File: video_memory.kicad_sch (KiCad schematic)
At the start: 23 parts

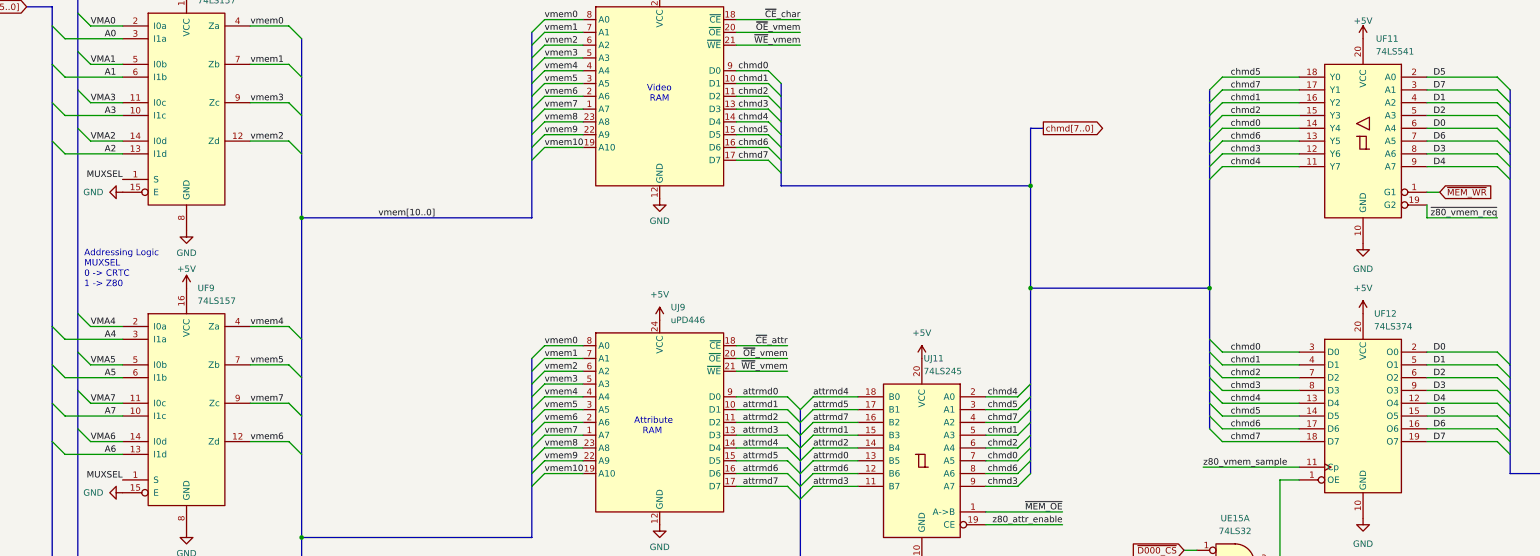
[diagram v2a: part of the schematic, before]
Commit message: pcb: finished IC routing
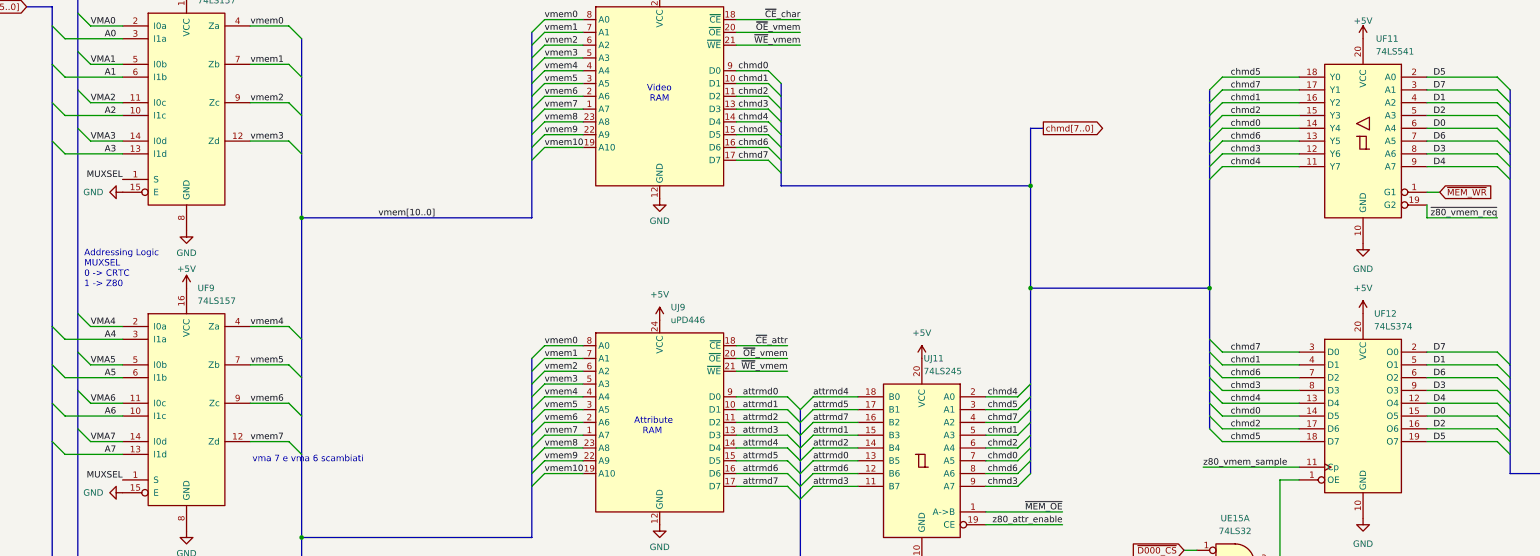
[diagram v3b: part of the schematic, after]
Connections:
- net A2: now also UF8.10 (I1c); no longer UF8.13 (I1d)
- net A3: now also UF8.13 (I1d); no longer UF8.10 (I1c)
- net A6: now also UF9.10 (I1c); no longer UF9.13 (I1d)
- net A7: now also UF9.13 (I1d); no longer UF9.10 (I1c)
- net D0: now also UF12.15 (O5); no longer UF12.2 (O0)
- net D2: now also UF12.16 (O6); no longer UF12.6 (O2)
- net D5: now also UF12.19 (O7); no longer UF12.15 (O5)
- net D6: now also UF12.6 (O2); no longer UF12.16 (O6)
- net D7: now also UF12.2 (O0); no longer UF12.19 (O7)
- net VMA2: now also UF8.11 (I0c); no longer UF8.14 (I0d)
- net VMA3: now also UF8.14 (I0d); no longer UF8.11 (I0c)
- net VMA6: now also UF9.11 (I0c); no longer UF9.14 (I0d)
- net VMA7: now also UF9.14 (I0d); no longer UF9.11 (I0c)
- net chmd0: now also UF12.14 (D5); no longer UF12.3 (D0)
- net chmd2: now also UF12.17 (D6); no longer UF12.7 (D2)
- net chmd5: now also UF12.18 (D7); no longer UF12.14 (D5)
- net chmd6: now also UF12.7 (D2); no longer UF12.17 (D6)
- net chmd7: now also UF12.3 (D0); no longer UF12.18 (D7)
- net vmem2: now also UF8.9 (Zc); no longer UF8.12 (Zd)
- net vmem3: now also UF8.12 (Zd); no longer UF8.9 (Zc)
- net vmem6: now also UF9.9 (Zc); no longer UF9.12 (Zd)
- net vmem7: now also UF9.12 (Zd); no longer UF9.9 (Zc)
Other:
- note added: "vma 7 e vma 6 scambiati"
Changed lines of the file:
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@@
 		)
 	)
+	(text "vma 7 e vma 6 scambiati"
+		(exclude_from_sim no)
+		(at 99.06 114.046 0)
+		(effects
+			(font
+				(size 1.27 1.27)
+			)
+		)
+	)
 	(text "Addressing Logic\nMUXSEL\n0 -> CRTC\n1 -> Z80"
 		(exclude_from_sim no)
@@
 		)
 	)
-	(label "VMA3"
+	(label "VMA2"
 		(at 55.88 43.18 0)
 		(effects
@@
 		)
 	)
-	(label "chmd0"
+	(label "chmd7"
 		(at 288.29 92.71 180)
 		(effects
@@
 		)
 	)
-	(label "chmd2"
+	(label "chmd6"
 		(at 288.29 97.79 180)
 		(effects
@@
 		)
 	)
-	(label "A6"
+	(label "A7"
 		(at 60.96 113.03 180)
 		(effects
@@
 		)
 	)
-	(label "chmd6"
+	(label "chmd2"
 		(at 288.29 107.95 180)
 		(effects
@@
 		)
 	)
-	(label "D2"
+	(label "D6"
 		(at 322.58 97.79 0)
 		(effects
@@
 		)
 	)
-	(label "VMA7"
+	(label "VMA6"
 		(at 55.88 102.87 0)
 		(effects
@@
 		)
 	)
-	(label "D0"
+	(label "D7"
 		(at 322.58 92.71 0)
 		(effects
@@
 		)
 	)
-	(label "vmem2"
+	(label "vmem3"
 		(at 87.63 50.8 0)
 		(effects
@@
 		)
 	)
-	(label "chmd7"
+	(label "chmd5"
 		(at 288.29 110.49 180)
 		(effects
@@
 		)
 	)
-	(label "D6"
+	(label "D2"
 		(at 322.58 107.95 0)
 		(effects
@@
 		)
 	)
-	(label "vmem7"
+	(label "vmem6"
 		(at 87.63 102.87 0)
 		(effects
@@
 		)
 	)
-	(label "D7"
+	(label "D5"
 		(at 322.58 110.49 0)
 		(effects
@@
 		)
 	)
-	(label "A3"
+	(label "A2"
 		(at 60.96 45.72 180)
 		(effects
@@
 		)
 	)
-	(label "VMA6"
+	(label "VMA7"
 		(at 55.88 110.49 0)
 		(effects
@@
 		)
 	)
-	(label "D5"
+	(label "D0"
 		(at 322.58 105.41 0)
 		(effects
@@
 		)
 	)
-	(label "VMA2"
+	(label "VMA3"
 		(at 55.88 50.8 0)
 		(effects
@@
 		)
 	)
-	(label "A7"
+	(label "A6"
 		(at 60.96 105.41 180)
 		(effects
@@
 		)
 	)
-	(label "chmd5"
+	(label "chmd0"
 		(at 288.29 105.41 180)
 		(effects
@@
 		)
 	)
-	(label "A2"
+	(label "A3"
 		(at 60.96 53.34 180)
 		(effects
@@
 		)
 	)
-	(label "vmem6"
+	(label "vmem7"
 		(at 87.63 110.49 0)
 		(effects
@@
 		)
 	)
-	(label "vmem3"
+	(label "vmem2"
 		(at 87.63 43.18 0)
 		(effects

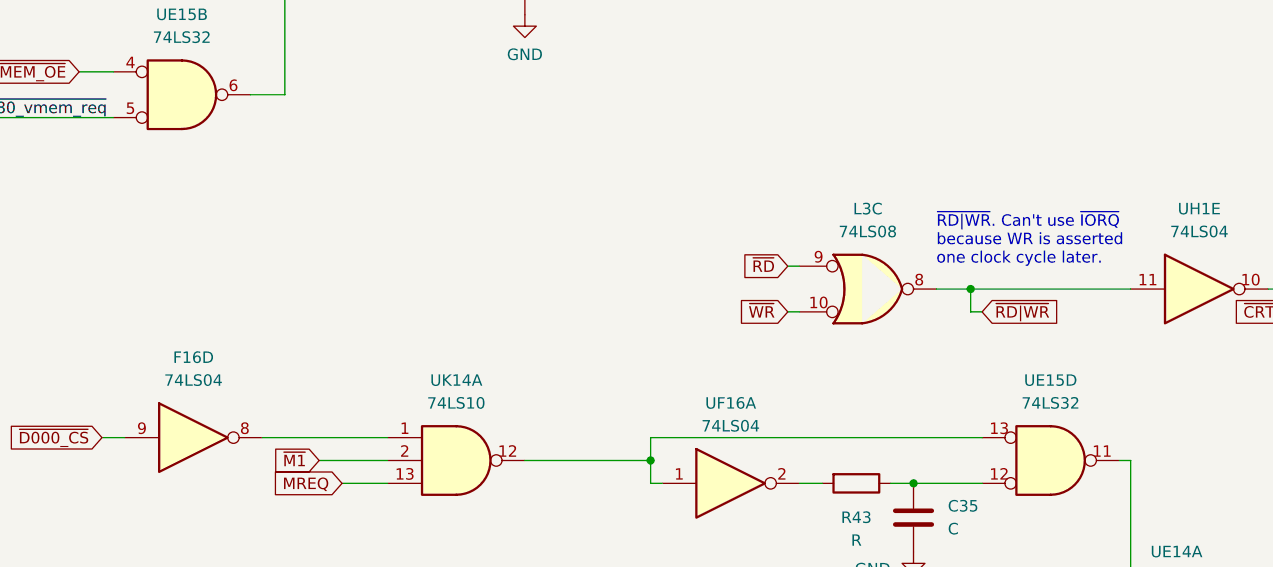
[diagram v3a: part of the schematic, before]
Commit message: pcb: added and placed almost all components
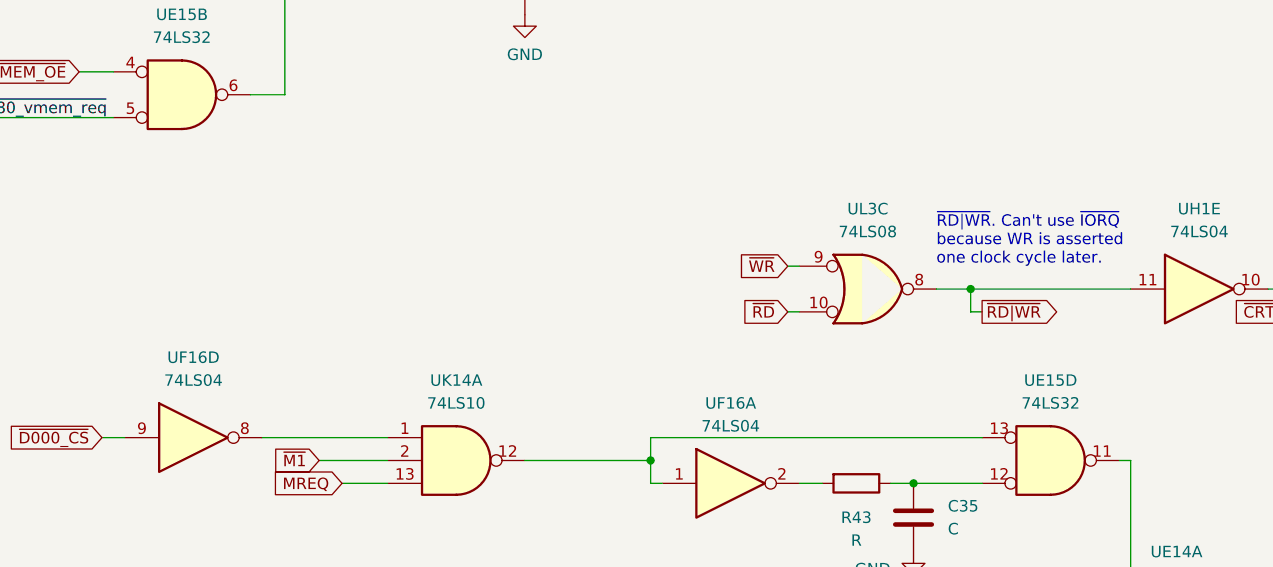
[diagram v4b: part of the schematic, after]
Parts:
- C35: footprint (none) -> Capacitor_THT:C_Disc_D4.3mm_W1.9mm_P5.00mm
- R43: footprint (none) -> Resistor_THT:R_Axial_DIN0204_L3.6mm_D1.6mm_P5.08mm_Vertical
- UF16: renamed from F16; footprint (none) -> Package_DIP:DIP-14_W7.62mm
- UL3: renamed from L3; footprint (none) -> Package_DIP:DIP-14_W7.62mm
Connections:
- net ~{RD}: now also UL3.10; no longer UL3.9
- net ~{WR}: now also UL3.9; no longer UL3.10
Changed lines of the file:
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@@
 	(wire
 		(pts
-			(xy 105.41 220.98) (xy 104.14 220.98)
+			(xy 105.41 215.9) (xy 104.14 215.9)
 		)
 		(stroke
@@
 	(wire
 		(pts
-			(xy 105.41 215.9) (xy 104.14 215.9)
+			(xy 105.41 220.98) (xy 104.14 220.98)
 		)
 		(stroke
@@
 	)
 	(global_label "~{RD|WR}"
-		(shape input)
+		(shape output)
 		(at 125.73 220.98 0)
 		(fields_autoplaced yes)
@@
 	(global_label "~{RD}"
 		(shape input)
-		(at 104.14 215.9 180)
+		(at 104.14 220.98 180)
 		(fields_autoplaced yes)
 		(effects
@@
 		)
 		(property "Intersheetrefs" "${INTERSHEET_REFS}"
-			(at 98.6148 215.9 0)
+			(at 98.6148 220.98 0)
 			(effects
 				(font
@@
 	(global_label "~{WR}"
 		(shape input)
-		(at 104.14 220.98 180)
+		(at 104.14 215.9 180)
 		(fields_autoplaced yes)
 		(effects
@@
 		)
 		(property "Intersheetrefs" "${INTERSHEET_REFS}"
-			(at 98.4334 220.98 0)
+			(at 98.4334 215.9 0)
 			(effects
 				(font
@@
 		(dnp no)
 		(fields_autoplaced yes)
-		(property "Reference" "L3"
+		(property "Reference" "UL3"
 			(at 113.03 209.55 0)
 			(effects
@@
 			)
 		)
-		(property "Footprint" ""
+		(property "Footprint" "Package_DIP:DIP-14_W7.62mm"
 			(at 113.03 218.44 0)
 			(effects
@@
 			(project "ceda"
 				(path "/12a6dbe3-008d-4c5b-88f6-9f1c816060be/3df68a1a-abd3-4ad7-9eb9-855dfc37a3a7"
-					(reference "L3")
+					(reference "UL3")
 					(unit 3)
 				)
@@
 			)
 		)
-		(property "Footprint" ""
+		(property "Footprint" "Capacitor_THT:C_Disc_D4.3mm_W1.9mm_P5.00mm"
 			(at 119.0752 247.65 0)
 			(effects
@@
 			)
 		)
-		(property "Footprint" ""
+		(property "Footprint" "Resistor_THT:R_Axial_DIN0204_L3.6mm_D1.6mm_P5.08mm_Vertical"
 			(at 111.76 238.252 90)
 			(effects
@@
 		(dnp no)
 		(fields_autoplaced yes)
-		(property "Reference" "F16"
+		(property "Reference" "UF16"
 			(at 38.1 226.06 0)
 			(effects
@@
 			)
 		)
-		(property "Footprint" ""
+		(property "Footprint" "Package_DIP:DIP-14_W7.62mm"
 			(at 38.1 234.95 0)
 			(effects
@@
 			(project "ceda"
 				(path "/12a6dbe3-008d-4c5b-88f6-9f1c816060be/3df68a1a-abd3-4ad7-9eb9-855dfc37a3a7"
-					(reference "F16")
+					(reference "UF16")
 					(unit 4)
 				)
